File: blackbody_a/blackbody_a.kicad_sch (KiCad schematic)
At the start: 0 parts

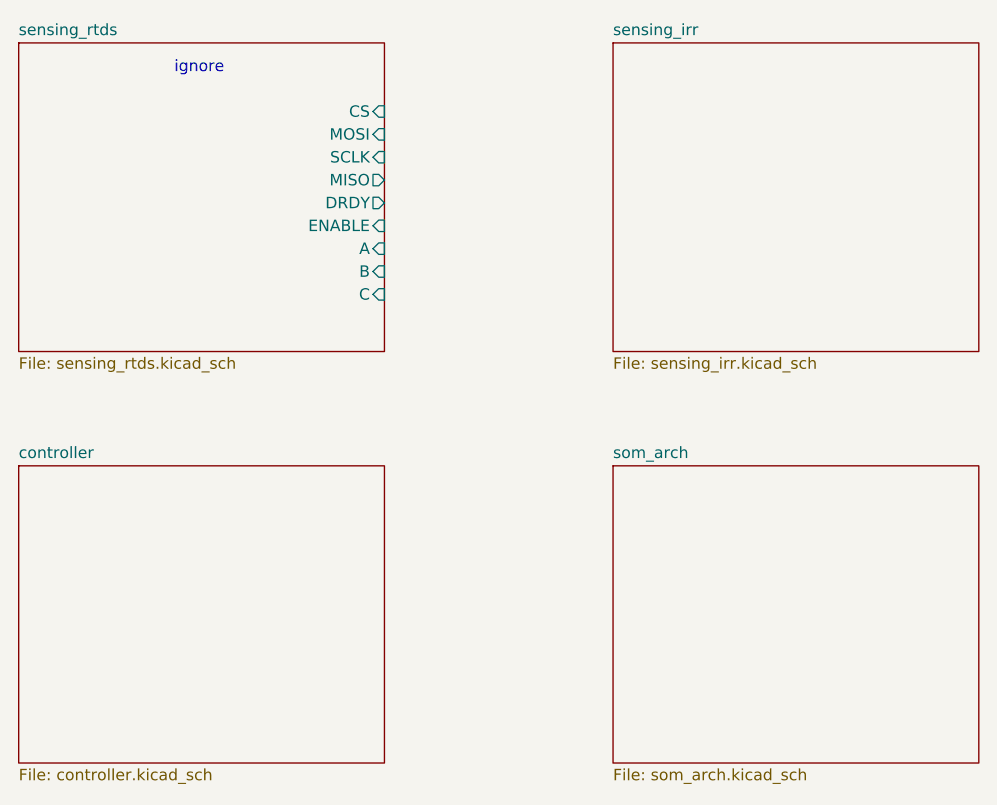
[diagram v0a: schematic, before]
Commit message: added more complexity + thermistor connection
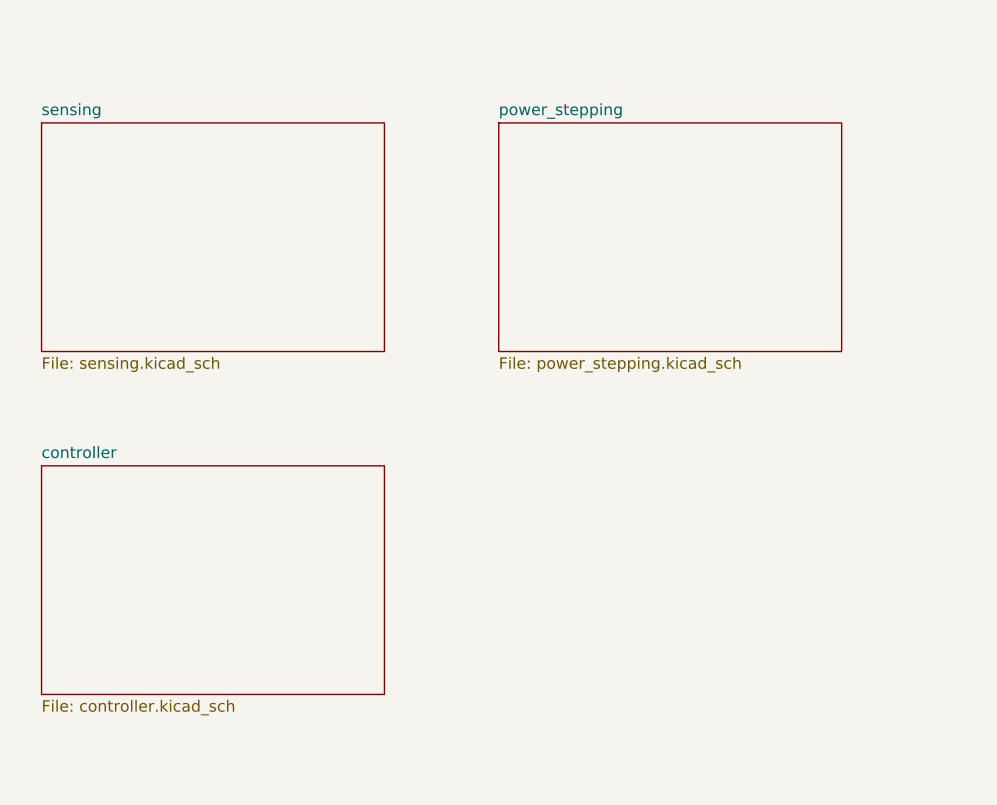
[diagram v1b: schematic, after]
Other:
- removed sheet sensing_irr
- removed sheet sensing_rtds
- removed sheet som_arch
- added sheet power_stepping (power_stepping.kicad_sch)
- added sheet sensing (sensing.kicad_sch)
- note removed: "ignore"
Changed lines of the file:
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@@
 	(generator_version "8.0")
 	(paper "A4")
-	(text "ignore"
-		(exclude_from_sim no)
-		(at 42.926 32.004 0)
-		(effects
-			(font
-				(size 1.27 1.27)
-			)
-		)
-	)
 	(sheet
-		(at 22.86 76.2)
-		(size 40.64 33.02)
+		(at 25.4 38.1)
+		(size 38.1 25.4)
 		(fields_autoplaced yes)
 		(stroke
@@
 			(color 0 0 0 0.0000)
 		)
-		(property "Sheetname" "controller"
-			(at 22.86 75.4884 0)
+		(property "Sheetname" "sensing"
+			(at 25.4 37.3884 0)
 			(effects
 				(font
@@
 			)
 		)
-		(property "Sheetfile" "controller.kicad_sch"
-			(at 22.86 109.8046 0)
+		(property "Sheetfile" "sensing.kicad_sch"
+			(at 25.4 64.0846 0)
 			(effects
 				(font
@@
 				)
 				(justify left top)
-			)
-		)
-		(instances
-			(project "blackbody_a"
-				(path "/1fc8ae43-742a-46b6-a93b-79253d0d0202"
-					(page "12")
-				)
-			)
-		)
-	)
-	(sheet
-		(at 88.9 29.21)
-		(size 40.64 34.29)
-		(fields_autoplaced yes)
-		(stroke
-			(width 0.1524)
-			(type solid)
-		)
-		(fill
-			(color 0 0 0 0.0000)
-		)
-		(property "Sheetname" "sensing_irr"
-			(at 88.9 28.4984 0)
-			(effects
-				(font
-					(size 1.27 1.27)
-				)
-				(justify left bottom)
-			)
-		)
-		(property "Sheetfile" "sensing_irr.kicad_sch"
-			(at 88.9 64.0846 0)
-			(effects
-				(font
-					(size 1.27 1.27)
-				)
-				(justify left top)
-			)
-		)
-		(instances
-			(project "blackbody_a"
-				(path "/1fc8ae43-742a-46b6-a93b-79253d0d0202"
-					(page "11")
-				)
-			)
-		)
-	)
-	(sheet
-		(at 22.86 29.21)
-		(size 40.64 34.29)
-		(fields_autoplaced yes)
-		(stroke
-			(width 0.1524)
-			(type solid)
-		)
-		(fill
-			(color 0 0 0 0.0000)
-		)
-		(property "Sheetname" "sensing_rtds"
-			(at 22.86 28.4984 0)
-			(effects
-				(font
-					(size 1.27 1.27)
-				)
-				(justify left bottom)
-			)
-		)
-		(property "Sheetfile" "sensing_rtds.kicad_sch"
-			(at 22.86 64.0846 0)
-			(effects
-				(font
-					(size 1.27 1.27)
-				)
-				(justify left top)
-			)
-		)
-		(pin "CS" input
-			(at 63.5 36.83 0)
-			(effects
-				(font
-					(size 1.27 1.27)
-				)
-				(justify right)
-			)
-		)
-		(pin "MOSI" input
-			(at 63.5 39.37 0)
-			(effects
-				(font
-					(size 1.27 1.27)
-				)
-				(justify right)
-			)
-		)
-		(pin "SCLK" input
-			(at 63.5 41.91 0)
-			(effects
-				(font
-					(size 1.27 1.27)
-				)
-				(justify right)
-			)
-		)
-		(pin "MISO" output
-			(at 63.5 44.45 0)
-			(effects
-				(font
-					(size 1.27 1.27)
-				)
-				(justify right)
-			)
-		)
-		(pin "DRDY" output
-			(at 63.5 46.99 0)
-			(effects
-				(font
-					(size 1.27 1.27)
-				)
-				(justify right)
-			)
-		)
-		(pin "ENABLE" input
-			(at 63.5 49.53 0)
-			(effects
-				(font
-					(size 1.27 1.27)
-				)
-				(justify right)
-			)
-		)
-		(pin "A" input
-			(at 63.5 52.07 0)
-			(effects
-				(font
-					(size 1.27 1.27)
-				)
-				(justify right)
-			)
-		)
-		(pin "B" input
-			(at 63.5 54.61 0)
-			(effects
-				(font
-					(size 1.27 1.27)
-				)
-				(justify right)
-			)
-		)
-		(pin "C" input
-			(at 63.5 57.15 0)
-			(effects
-				(font
-					(size 1.27 1.27)
-				)
-				(justify right)
 			)
 		)
@@
 	)
 	(sheet
-		(at 88.9 76.2)
-		(size 40.64 33.02)
+		(at 76.2 38.1)
+		(size 38.1 25.4)
 		(fields_autoplaced yes)
 		(stroke
@@
 			(color 0 0 0 0.0000)
 		)
-		(property "Sheetname" "som_arch"
-			(at 88.9 75.4884 0)
+		(property "Sheetname" "power_stepping"
+			(at 76.2 37.3884 0)
 			(effects
 				(font
@@
 			)
 		)
-		(property "Sheetfile" "som_arch.kicad_sch"
-			(at 88.9 109.8046 0)
+		(property "Sheetfile" "power_stepping.kicad_sch"
+			(at 76.2 64.0846 0)
 			(effects
 				(font
@@
 			(project "blackbody_a"
 				(path "/1fc8ae43-742a-46b6-a93b-79253d0d0202"
-					(page "13")
+					(page "4")
 				)
 			)
+		)
+	)
+	(sheet
+		(at 25.4 76.2)
+		(size 38.1 25.4)
+		(fields_autoplaced yes)
+		(stroke
+			(width 0.1524)
+			(type solid)
+		)
+		(fill
+			(color 0 0 0 0.0000)
+		)
+		(property "Sheetname" "controller"
+			(at 25.4 75.4884 0)
+			(effects
+				(font
+					(size 1.27 1.27)
+				)
+				(justify left bottom)
+			)
+		)
+		(property "Sheetfile" "controller.kicad_sch"
+			(at 25.4 102.1846 0)
+			(effects
+				(font
+					(size 1.27 1.27)
+				)
+				(justify left top)
+			)
+		)
+		(instances
+			(project "blackbody_a"
+				(path "/1fc8ae43-742a-46b6-a93b-79253d0d0202"
+					(page "3")
+				)
+			)

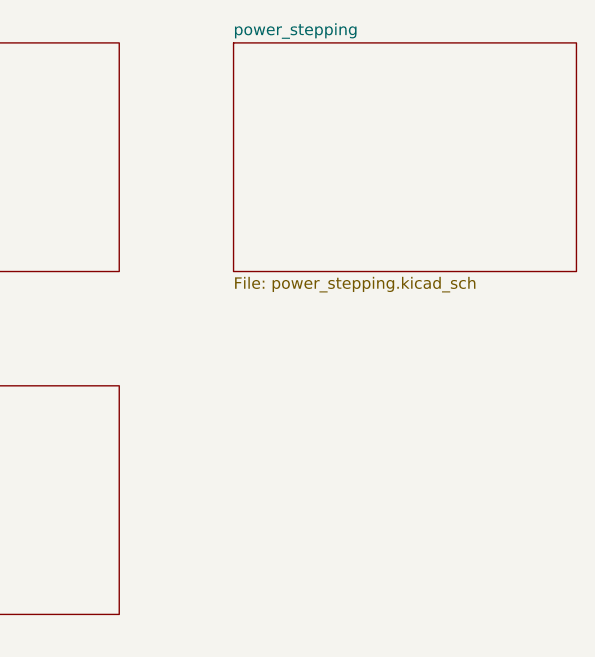
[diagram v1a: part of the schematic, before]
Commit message: Added controller and CAN
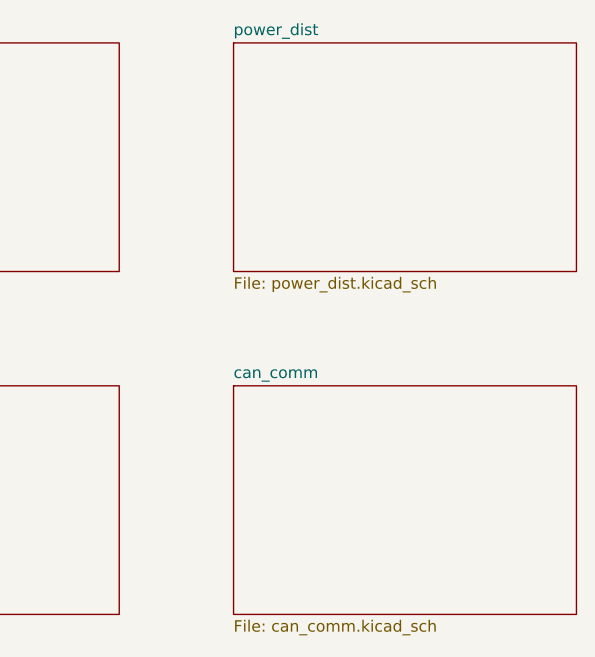
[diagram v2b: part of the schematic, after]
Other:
- removed sheet power_stepping
- added sheet can_comm (can_comm.kicad_sch)
- added sheet power_dist (power_dist.kicad_sch)
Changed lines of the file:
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@@
 			(color 0 0 0 0.0000)
 		)
-		(property "Sheetname" "power_stepping"
+		(property "Sheetname" "power_dist"
 			(at 76.2 37.3884 0)
 			(effects
@@
 			)
 		)
-		(property "Sheetfile" "power_stepping.kicad_sch"
+		(property "Sheetfile" "power_dist.kicad_sch"
 			(at 76.2 64.0846 0)
 			(effects
@@
 			(project "blackbody_a"
 				(path "/1fc8ae43-742a-46b6-a93b-79253d0d0202"
-					(page "4")
+					(page "5")
 				)
 			)
@@
 				)
 			)
+		)
+	)
+	(sheet
+		(at 76.2 76.2)
+		(size 38.1 25.4)
+		(fields_autoplaced yes)
+		(stroke
+			(width 0.1524)
+			(type solid)
+		)
+		(fill
+			(color 0 0 0 0.0000)
+		)
+		(property "Sheetname" "can_comm"
+			(at 76.2 75.4884 0)
+			(effects
+				(font
+					(size 1.27 1.27)
+				)
+				(justify left bottom)
+			)
+		)
+		(property "Sheetfile" "can_comm.kicad_sch"
+			(at 76.2 102.1846 0)
+			(effects
+				(font
+					(size 1.27 1.27)
+				)
+				(justify left top)
+			)
+		)
+		(instances
+			(project "blackbody_a"
+				(path "/1fc8ae43-742a-46b6-a93b-79253d0d0202"
+					(page "5")
+				)
+			)

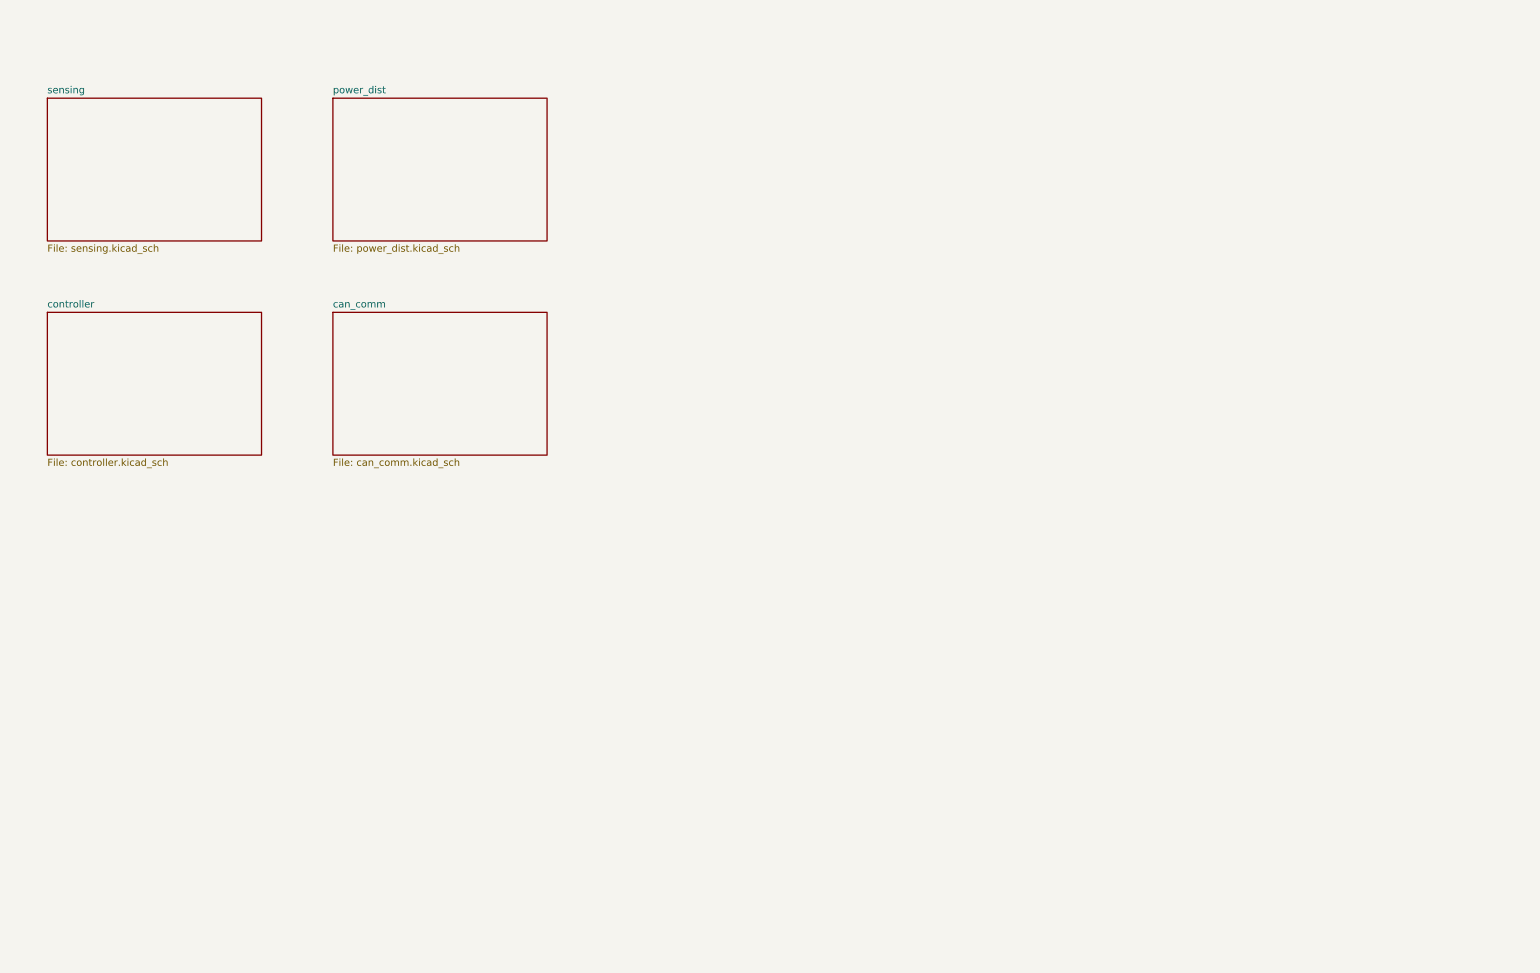
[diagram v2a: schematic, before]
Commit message: Added power distribution
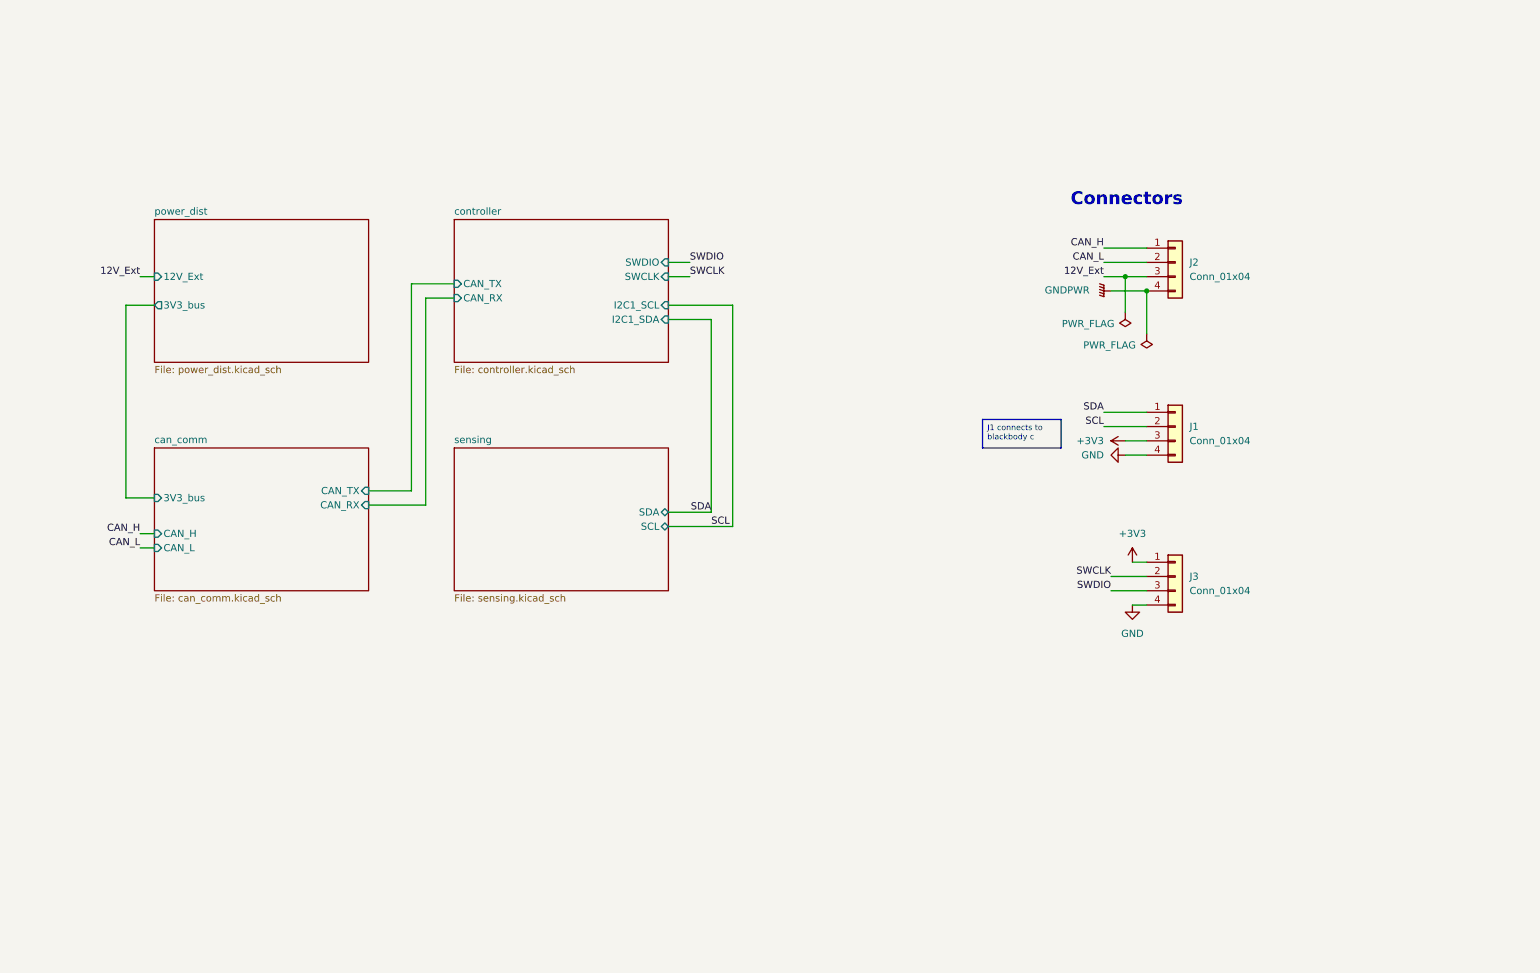
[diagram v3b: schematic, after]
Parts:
- added J1, J2, J3: Conn_01x04, symbol Connector_Generic:Conn_01x04
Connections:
- new net +3V3: J1.3 (Pin_3), J3.1 (Pin_1)
- new net 12V_Ext: J2.3 (Pin_3)
- new net CAN_H: J2.1 (Pin_1)
- new net CAN_L: J2.2 (Pin_2)
- new net GND: J1.4 (Pin_4), J3.4 (Pin_4)
- new net GNDPWR: J2.4 (Pin_4)
- new net SCL: J1.2 (Pin_2)
- new net SDA: J1.1 (Pin_1)
- new net SWCLK: J3.2 (Pin_2)
- new net SWDIO: J3.3 (Pin_3)
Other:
- sheet can_comm ports: added 3V3_bus, CAN_H, CAN_L, CAN_RX, CAN_TX; removed none
- sheet controller ports: added CAN_RX, CAN_TX, I2C1_SCL, I2C1_SDA, SWCLK, SWDIO; removed none
- sheet power_dist ports: added 12V_Ext, 3V3_bus; removed none
- sheet sensing ports: added SCL, SDA; removed none
- note added: "Connectors"

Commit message: minor errors
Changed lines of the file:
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@@
 	(generator_version "8.0")
 	(paper "A4")
-	(junction
-		(at 220.98 72.39)
-		(diameter 0)
-		(color 0 0 0 0)
-	)
-	(junction
-		(at 217.17 69.85)
-		(diameter 0)
-		(color 0 0 0 0)
-	)
 	(wire
 		(pts
@@
 	(wire
 		(pts
-			(xy 217.17 69.85) (xy 220.98 69.85)
-		)
-		(stroke
-			(width 0)
-			(type default)
-		)
-	)
-	(wire
-		(pts
 			(xy 147.32 114.3) (xy 147.32 74.93)
 		)
@@
 	(wire
 		(pts
-			(xy 217.17 69.85) (xy 217.17 76.2)
-		)
-		(stroke
-			(width 0)
-			(type default)
-		)
-	)
-	(wire
-		(pts
 			(xy 143.51 77.47) (xy 143.51 111.76)
 		)
@@
 	(wire
 		(pts
-			(xy 213.36 69.85) (xy 217.17 69.85)
-		)
-		(stroke
-			(width 0)
-			(type default)
-		)
-	)
-	(wire
-		(pts
-			(xy 220.98 80.01) (xy 220.98 72.39)
+			(xy 213.36 69.85) (xy 220.98 69.85)
 		)
 		(stroke
@@
 	)
 	(symbol
-		(lib_id "power:PWR_FLAG")
-		(at 220.98 80.01 180)
-		(unit 1)
-		(exclude_from_sim no)
-		(in_bom yes)
-		(on_board yes)
-		(dnp no)
-		(property "Reference" "#FLG02"
-			(at 220.98 81.915 0)
-			(effects
-				(font
-					(size 1.27 1.27)
-				)
-				(hide yes)
-			)
-		)
-		(property "Value" "PWR_FLAG"
-			(at 214.376 82.042 0)
-			(effects
-				(font
-					(size 1.27 1.27)
-				)
-			)
-		)
-		(property "Footprint" ""
-			(at 220.98 80.01 0)
-			(effects
-				(font
-					(size 1.27 1.27)
-				)
-				(hide yes)
-			)
-		)
-		(property "Datasheet" "~"
-			(at 220.98 80.01 0)
-			(effects
-				(font
-					(size 1.27 1.27)
-				)
-				(hide yes)
-			)
-		)
-		(property "Description" "Special symbol for telling ERC where power comes from"
-			(at 220.98 80.01 0)
-			(effects
-				(font
-					(size 1.27 1.27)
-				)
-				(hide yes)
-			)
-		)
-		(pin "1"
-		)
-		(instances
-			(project "blackbody_a"
-				(path "/1fc8ae43-742a-46b6-a93b-79253d0d0202"
-					(reference "#FLG02")
-					(unit 1)
-				)
-			)
-		)
-	)
-	(symbol
 		(lib_id "Connector_Generic:Conn_01x04")
 		(at 226.06 96.52 0)
@@
 				(path "/1fc8ae43-742a-46b6-a93b-79253d0d0202"
 					(reference "J1")
-					(unit 1)
-				)
-			)
-		)
-	)
-	(symbol
-		(lib_id "power:PWR_FLAG")
-		(at 217.17 76.2 180)
-		(unit 1)
-		(exclude_from_sim no)
-		(in_bom yes)
-		(on_board yes)
-		(dnp no)
-		(property "Reference" "#FLG03"
-			(at 217.17 78.105 0)
-			(effects
-				(font
-					(size 1.27 1.27)
-				)
-				(hide yes)
-			)
-		)
-		(property "Value" "PWR_FLAG"
-			(at 210.566 78.232 0)
-			(effects
-				(font
-					(size 1.27 1.27)
-				)
-			)
-		)
-		(property "Footprint" ""
-			(at 217.17 76.2 0)
-			(effects
-				(font
-					(size 1.27 1.27)
-				)
-				(hide yes)
-			)
-		)
-		(property "Datasheet" "~"
-			(at 217.17 76.2 0)
-			(effects
-				(font
-					(size 1.27 1.27)
-				)
-				(hide yes)
-			)
-		)
-		(property "Description" "Special symbol for telling ERC where power comes from"
-			(at 217.17 76.2 0)
-			(effects
-				(font
-					(size 1.27 1.27)
-				)
-				(hide yes)
-			)
-		)
-		(pin "1"
-		)
-		(instances
-			(project "blackbody_a"
-				(path "/1fc8ae43-742a-46b6-a93b-79253d0d0202"
-					(reference "#FLG03")
 					(unit 1)
 				)
@@
 			)
 		)
-		(pin "SDA" bidirectional
+		(pin "SDA" output
 			(at 135.89 111.76 0)
 			(effects
@@
 			)
 		)
-		(pin "SCL" bidirectional
+		(pin "SCL" output
 			(at 135.89 114.3 0)
 			(effects
